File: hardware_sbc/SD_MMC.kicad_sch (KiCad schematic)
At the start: 14 parts, among them J10 Micro_SD_Card, U1I IMX8MM, U7 SDINBDG4-8G

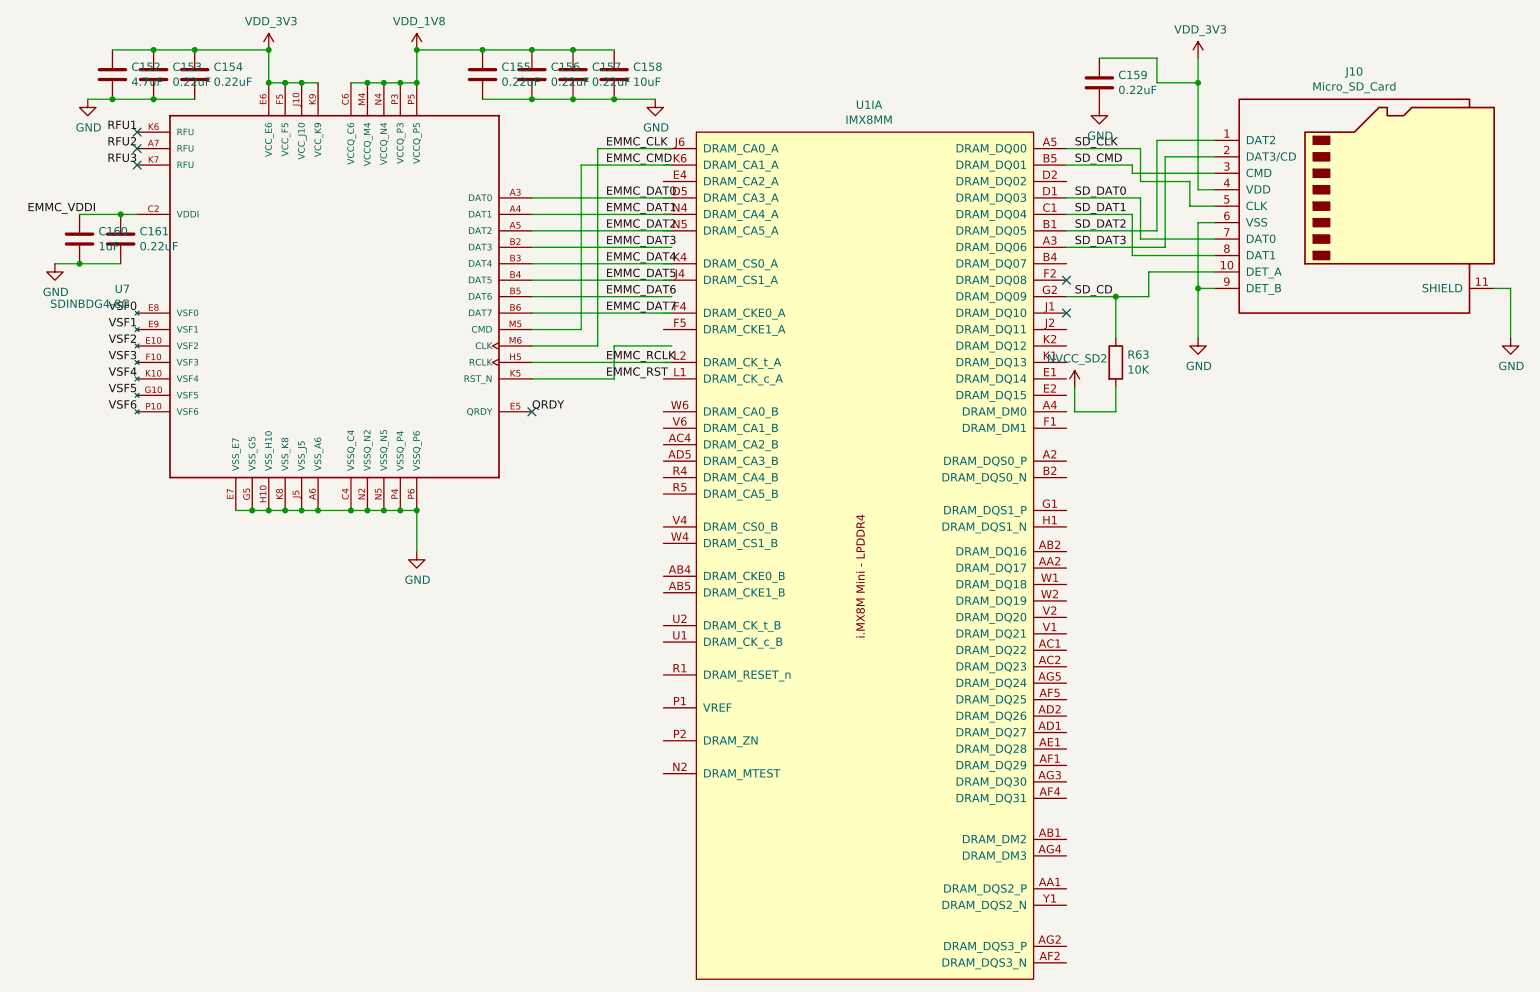
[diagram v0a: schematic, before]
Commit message: Updated production files and fixed schematic link issue.
Fixed schematic unit number issue and re-linked to PCB.
New gerbers, STEP file, schematic PDF.
Deleted old KiCAD 6 files.
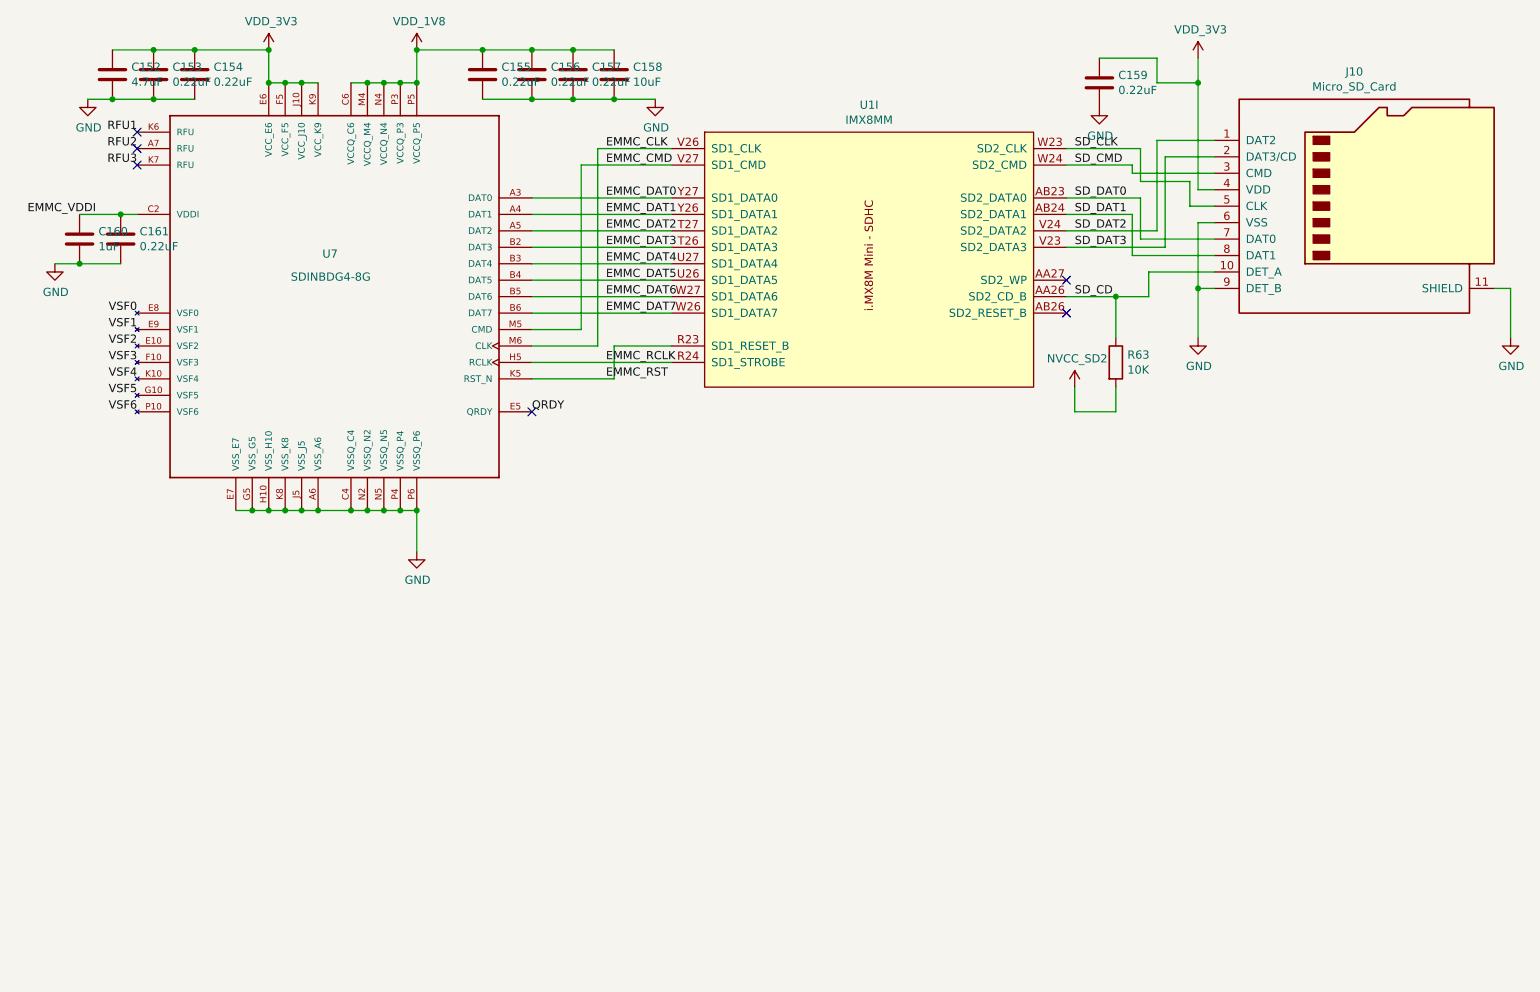
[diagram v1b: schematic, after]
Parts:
- renumbered U1I to U1
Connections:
- net EMMC_CLK: now also U1.V26 (SD1_CLK)
- net EMMC_CMD: now also U1.V27 (SD1_CMD)
- net EMMC_DAT0: now also U1.Y27 (SD1_DATA0)
- net EMMC_DAT1: now also U1.Y26 (SD1_DATA1)
- net EMMC_DAT2: now also U1.T27 (SD1_DATA2)
- net EMMC_DAT3: now also U1.T26 (SD1_DATA3)
- net EMMC_DAT4: now also U1.U27 (SD1_DATA4)
- net EMMC_DAT5: now also U1.U26 (SD1_DATA5)
- net EMMC_DAT6: now also U1.W27 (SD1_DATA6)
- net EMMC_DAT7: now also U1.W26 (SD1_DATA7)
- net EMMC_RCLK: now also U1.R24 (SD1_STROBE)
- net EMMC_RST: now also U1.R23 (SD1_RESET_B)
- net SD_CD: now also U1.AA26 (SD2_CD_B); no longer U1.G2 (DRAM_DQ09)
- net SD_CLK: now also U1.W23 (SD2_CLK); no longer U1.A5 (DRAM_DQ00)
- net SD_CMD: now also U1.W24 (SD2_CMD); no longer U1.B5 (DRAM_DQ01)
- net SD_DAT0: now also U1.AB23 (SD2_DATA0); no longer U1.D1 (DRAM_DQ03)
- net SD_DAT1: now also U1.AB24 (SD2_DATA1); no longer U1.C1 (DRAM_DQ04)
- net SD_DAT2: now also U1.V24 (SD2_DATA2); no longer U1.B1 (DRAM_DQ05)
- net SD_DAT3: now also U1.V23 (SD2_DATA3); no longer U1.A3 (DRAM_DQ06)
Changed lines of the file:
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@@
 	(label "VSF3"
 		(at 95.25 149.86 180)
+		(fields_autoplaced yes)
 		(effects
 			(font
@@
 	(label "EMMC_RST"
 		(at 167.64 152.4 0)
+		(fields_autoplaced yes)
 		(effects
 			(font
@@
 	(label "VSF4"
 		(at 95.25 152.4 180)
+		(fields_autoplaced yes)
 		(effects
 			(font
@@
 	(label "SD_DAT0"
 		(at 240.03 124.46 0)
+		(fields_autoplaced yes)
 		(effects
 			(font
@@
 	(label "RFU2"
 		(at 95.25 116.84 180)
+		(fields_autoplaced yes)
 		(effects
 			(font
@@
 	(label "VSF0"
 		(at 95.25 142.24 180)
+		(fields_autoplaced yes)
 		(effects
 			(font
@@
 	(label "EMMC_DAT2"
 		(at 167.64 129.54 0)
+		(fields_autoplaced yes)
 		(effects
 			(font
@@
 	(label "EMMC_RCLK"
 		(at 167.64 149.86 0)
+		(fields_autoplaced yes)
 		(effects
 			(font
@@
 	(label "EMMC_VDDI"
 		(at 88.9 127 180)
+		(fields_autoplaced yes)
 		(effects
 			(font
@@
 	(label "SD_DAT3"
 		(at 240.03 132.08 0)
+		(fields_autoplaced yes)
 		(effects
 			(font
@@
 	(label "EMMC_DAT7"
 		(at 167.64 142.24 0)
+		(fields_autoplaced yes)
 		(effects
 			(font
@@
 	(label "SD_CD"
 		(at 240.03 139.7 0)
+		(fields_autoplaced yes)
 		(effects
 			(font
@@
 	(label "EMMC_CMD"
 		(at 167.64 119.38 0)
+		(fields_autoplaced yes)
 		(effects
 			(font
@@
 	(label "EMMC_DAT1"
 		(at 167.64 127 0)
+		(fields_autoplaced yes)
 		(effects
 			(font
@@
 	(label "VSF2"
 		(at 95.25 147.32 180)
+		(fields_autoplaced yes)
 		(effects
 			(font
@@
 	(label "EMMC_DAT5"
 		(at 167.64 137.16 0)
+		(fields_autoplaced yes)
 		(effects
 			(font
@@
 	(label "EMMC_CLK"
 		(at 167.64 116.84 0)
+		(fields_autoplaced yes)
 		(effects
 			(font
@@
 	(label "SD_CLK"
 		(at 240.03 116.84 0)
+		(fields_autoplaced yes)
 		(effects
 			(font
@@
 	(label "EMMC_DAT4"
 		(at 167.64 134.62 0)
+		(fields_autoplaced yes)
 		(effects
 			(font
@@
 	(label "EMMC_DAT0"
 		(at 167.64 124.46 0)
+		(fields_autoplaced yes)
 		(effects
 			(font
@@
 	(label "QRDY"
 		(at 156.21 157.48 0)
+		(fields_autoplaced yes)
 		(effects
 			(font
@@
 	(label "SD_DAT1"
 		(at 240.03 127 0)
+		(fields_autoplaced yes)
 		(effects
 			(font
@@
 	(label "EMMC_DAT6"
 		(at 167.64 139.7 0)
+		(fields_autoplaced yes)
 		(effects
 			(font
@@
 	(label "VSF1"
 		(at 95.25 144.78 180)
+		(fields_autoplaced yes)
 		(effects
 			(font
@@
 	(label "EMMC_DAT3"
 		(at 167.64 132.08 0)
+		(fields_autoplaced yes)
 		(effects
 			(font
@@
 	(label "RFU1"
 		(at 95.25 114.3 180)
+		(fields_autoplaced yes)
 		(effects
 			(font
@@
 	(label "RFU3"
 		(at 95.25 119.38 180)
+		(fields_autoplaced yes)
 		(effects
 			(font
@@
 	(label "VSF6"
 		(at 95.25 157.48 180)
+		(fields_autoplaced yes)
 		(effects
 			(font
@@
 	(label "SD_DAT2"
 		(at 240.03 129.54 0)
+		(fields_autoplaced yes)
 		(effects
 			(font
@@
 	(label "VSF5"
 		(at 95.25 154.94 180)
+		(fields_autoplaced yes)
 		(effects
 			(font
@@
 	(label "SD_CMD"
 		(at 240.03 119.38 0)
+		(fields_autoplaced yes)
 		(effects
 			(font
@@
 		(lib_id "mxenc:MIMX8MM6DVTLZAA")
 		(at 208.28 182.88 0)
-		(unit 1)
+		(unit 9)
 		(exclude_from_sim no)
 		(in_bom yes)
 		(on_board yes)
 		(dnp no)
-		(property "Reference" "U1I"
+		(property "Reference" "U1"
 			(at 208.28 110.109 0)
 			(effects
@@
 			(project "kimchi_micro"
 				(path "/394ea9d6-84ac-414f-b42c-59edf258c746/00000000-0000-0000-0000-00005dad658f"
-					(reference "U1I")
-					(unit 1)
+					(reference "U1")
+					(unit 9)
 				)
 			)
@@
 	)
 	(symbol
-		(lib_name "mxenc:SDINBDG4-8G")
 		(lib_id "mxenc:SDINBDG4-8G")
 		(at 125.73 139.7 0)
@@
 		(dnp no)
 		(property "Reference" "U7"
-			(at 94.1578 138.5316 0)
+			(at 126.238 133.096 0)
 			(effects
 				(font
@@
 		)
 		(property "Value" "SDINBDG4-8G"
-			(at 94.1578 140.843 0)
+			(at 131.318 136.652 0)
 			(effects
 				(font
